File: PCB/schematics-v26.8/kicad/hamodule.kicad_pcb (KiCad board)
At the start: 4 copper layers, 129.6 x 83.3 mm, 203 parts, among them J1 GND|5V, J10 Tx|Rx, J11 Sda|Scl, J12 3|9, J13 13|12, J14 3.3v|GND|7|15, J15 2604-1104, J16 2604-1104, J17 TestPoint, J19 TestPoint, J2 2604-1102, J3 USB_C_Receptacle_USB2.0, J4 GND|3.3V, J5 Jumper 3.3v, J6 2604-1104, J7 2604-1104, J8 5v|GND|Do, J9 Screen, K1 AQG22205, K2 AQG22205, K3 AQG22205, K4 AQG22205, K5 AQG22205, K6 AQG22205, K7 AQG22205, K8 AQG22205, SW1 USB | PS, SW2 Reset, SW3 Boot, U1 LD1117AV33, U10 SN74LV1T34DBV, U11 ULN2803A, U12 TCAL6416, U14 74AHC1G04, U2 USBLC6-2SC6, U3 ESP32-S3-WROOM-2, U4 LDA210, U5 LDA210, U6 LDA210, U7 LDA210, U8 SHT4x, U9 SN74LVCH8T245

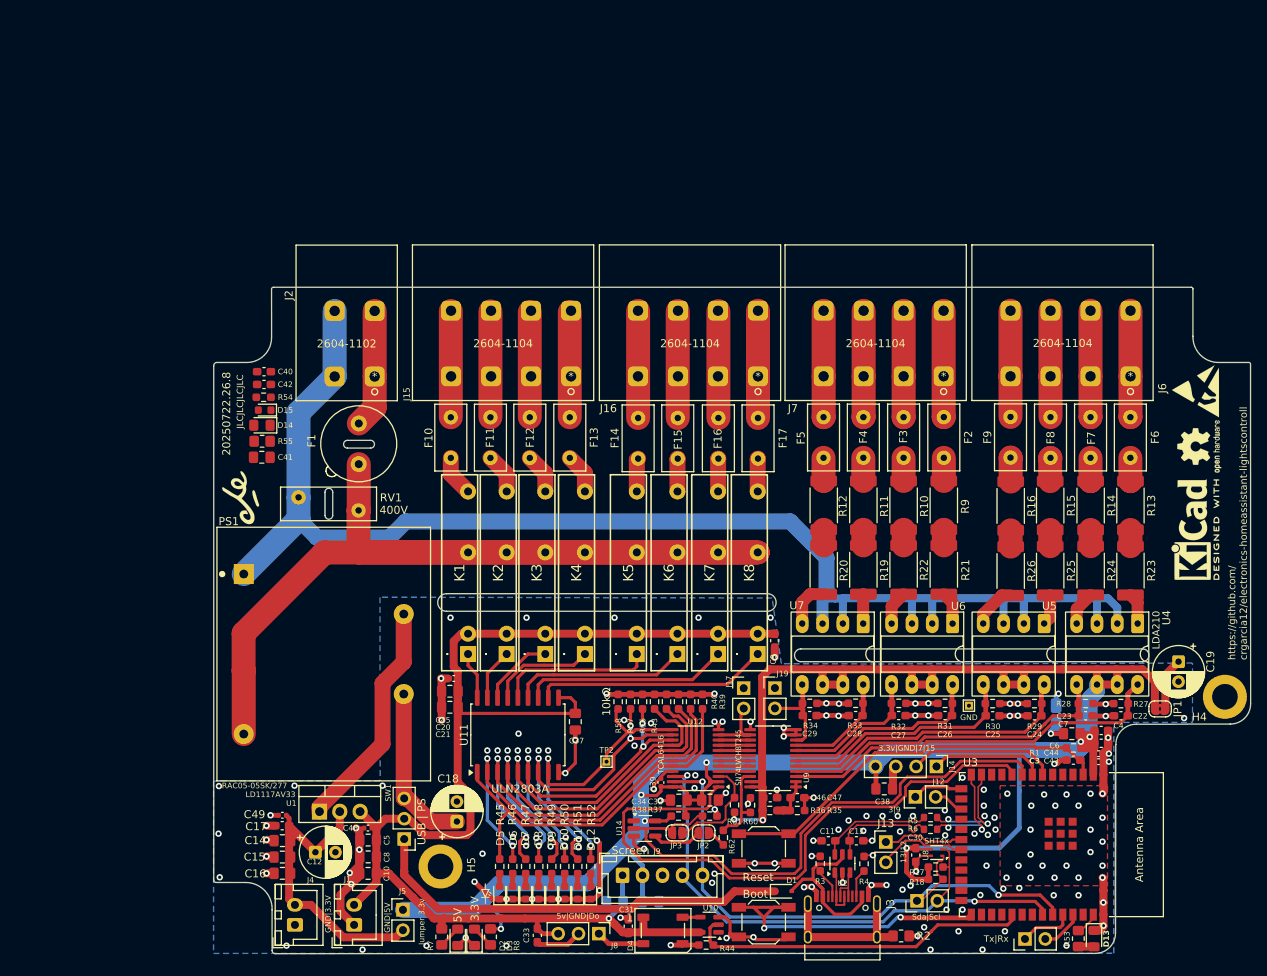
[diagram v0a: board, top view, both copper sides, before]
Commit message: Created only one project specific symbol library, one for footprints, and one for icons. Deleted all the rest from the components folder
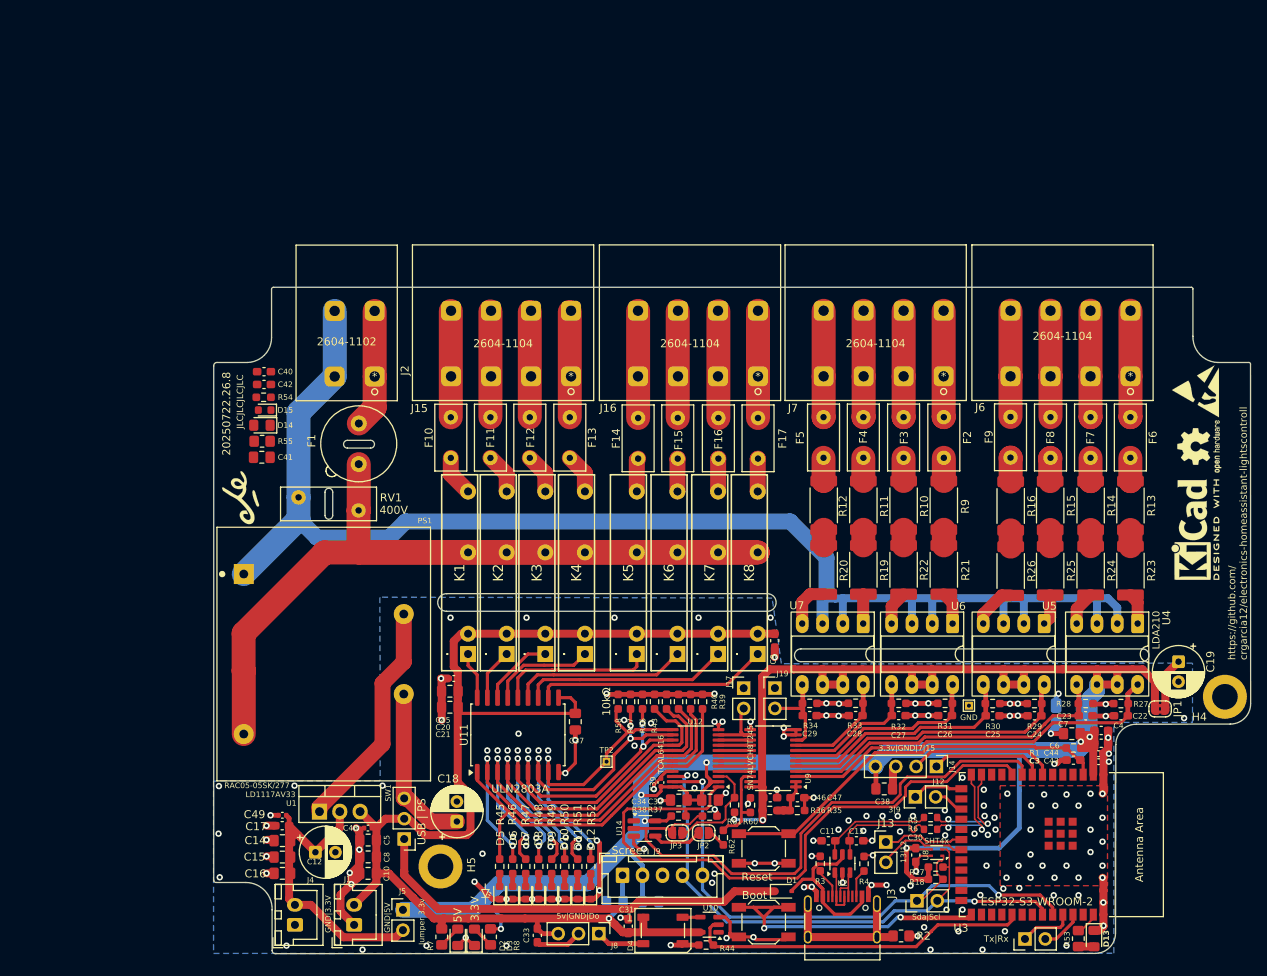
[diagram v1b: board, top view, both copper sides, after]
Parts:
- F10, F11, F12, F13, F14, F15, F16, F17, F2, F3, F4, F5, F6, F7, F8, F9: footprint RST-80-AMMO:FUSE_RST-1-BULK -> Hamodule_Footprints:FUSE_RST-1-BULK
- G1: footprint icons:depsi -> Hamodule_Icons_Footprints:depsi
- G10: footprint icons:che -> Hamodule_Icons_Footprints:che
- G2: footprint icons:flags -> Hamodule_Icons_Footprints:flags
- G3: footprint icons:qr_code_m -> Hamodule_Icons_Footprints:qr_code_m
- G4: footprint icons:led_6000dpi -> Hamodule_Icons_Footprints:led_6000dpi
- G5: footprint icons:danger1_negative -> Hamodule_Icons_Footprints:danger1_negative
- J15, J16, J6, J7: footprint wago-2604-1104:big_pads_2604-1104 -> Hamodule_Footprints:WAGO_2604-1104
- J2: footprint wago-2604-1102:big_pads_2604-1102 -> Hamodule_Footprints:WAGO-2604-1102
- J3: footprint usb-c:USB_C_Receptacle_HRO_TYPE-C-31-M-12 -> Connector_USB:USB_C_Receptacle_HRO_TYPE-C-31-M-12
- K1, K2, K3, K4, K5, K6, K7, K8: footprint AQG12205:AQG12205 -> Hamodule_Footprints:AQG12205
- PS1: footprint rac05-05sk:277 -> Hamodule_Footprints:RAC05-05SK_277
- SW2, SW3: footprint hamodule_SW_SPST_SKQG_WithStem:SW_SPST_SKQG_WithStem -> Button_Switch_SMD:SW_SPST_SKQG_WithStem
- U3: footprint Espressif:ESP32-S3-WROOM-2 -> Hamodule_Footprints:ESP32-S3-WROOM-2

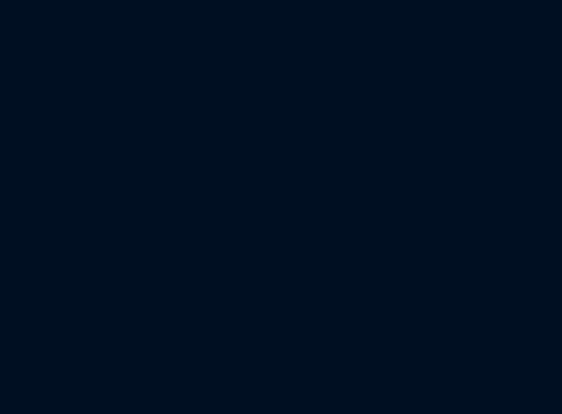
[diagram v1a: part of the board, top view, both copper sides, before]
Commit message: Created symbols for every image and logo, in order there are no warnings
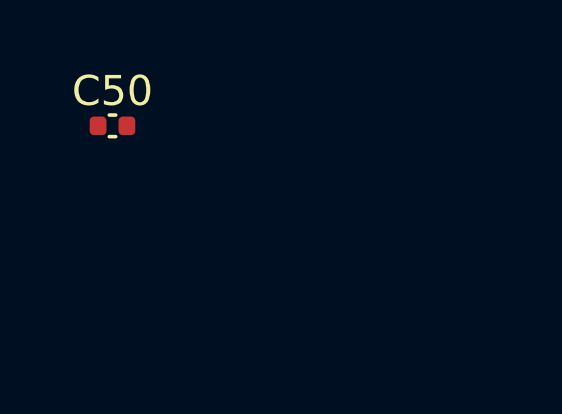
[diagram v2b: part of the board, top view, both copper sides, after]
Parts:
- added C50: 10uF, Capacitor_SMD:C_0402_1005Metric, F.Cu at (0.94, 0.48)
- G1: value LOGO -> Depsi
- G10: value LOGO -> Che
- G2: value LOGO -> Flags
- G3: value LOGO -> Qr Code; footprint Hamodule_Icons_Footprints:qr_code_m -> Hamodule_Icons_Footprints:qr_code
- G4: value LOGO -> Led; footprint Hamodule_Icons_Footprints:led_6000dpi -> Hamodule_Icons_Footprints:led
- G5: value LOGO -> Danger; footprint Hamodule_Icons_Footprints:danger1_negative -> Hamodule_Icons_Footprints:danger
- G6: value KiCad-Logo2_5mm_SilkScreen -> KiCad
- G7: value OSHW-Logo2_7.3x6mm_SilkScreen -> OSHW
- G8: value ESD-Logo_6.6x6mm_SilkScreen -> Esd

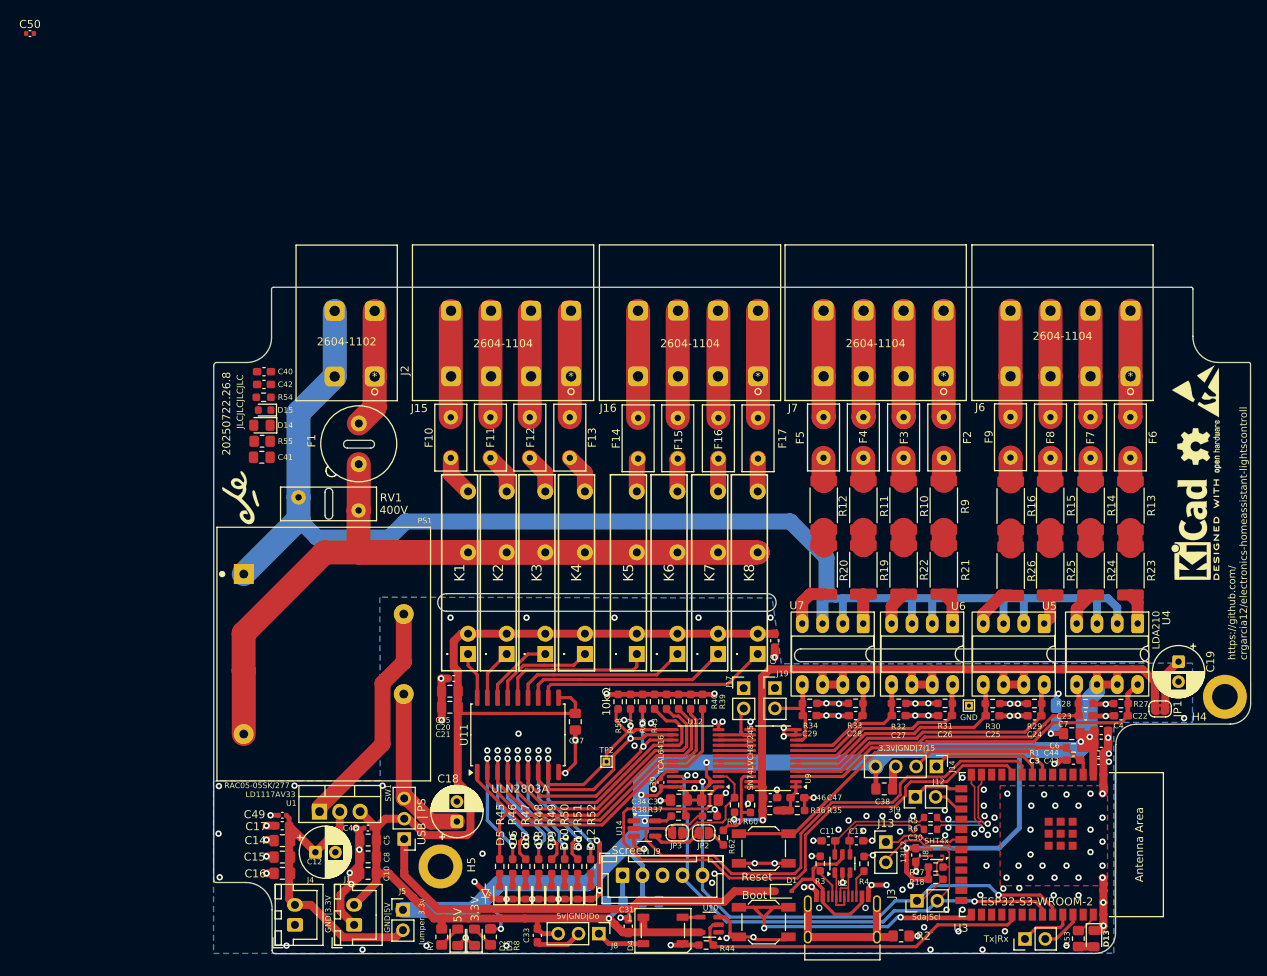
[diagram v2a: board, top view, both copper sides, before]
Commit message: Adding new spare part: C50 - 0402 capacitor
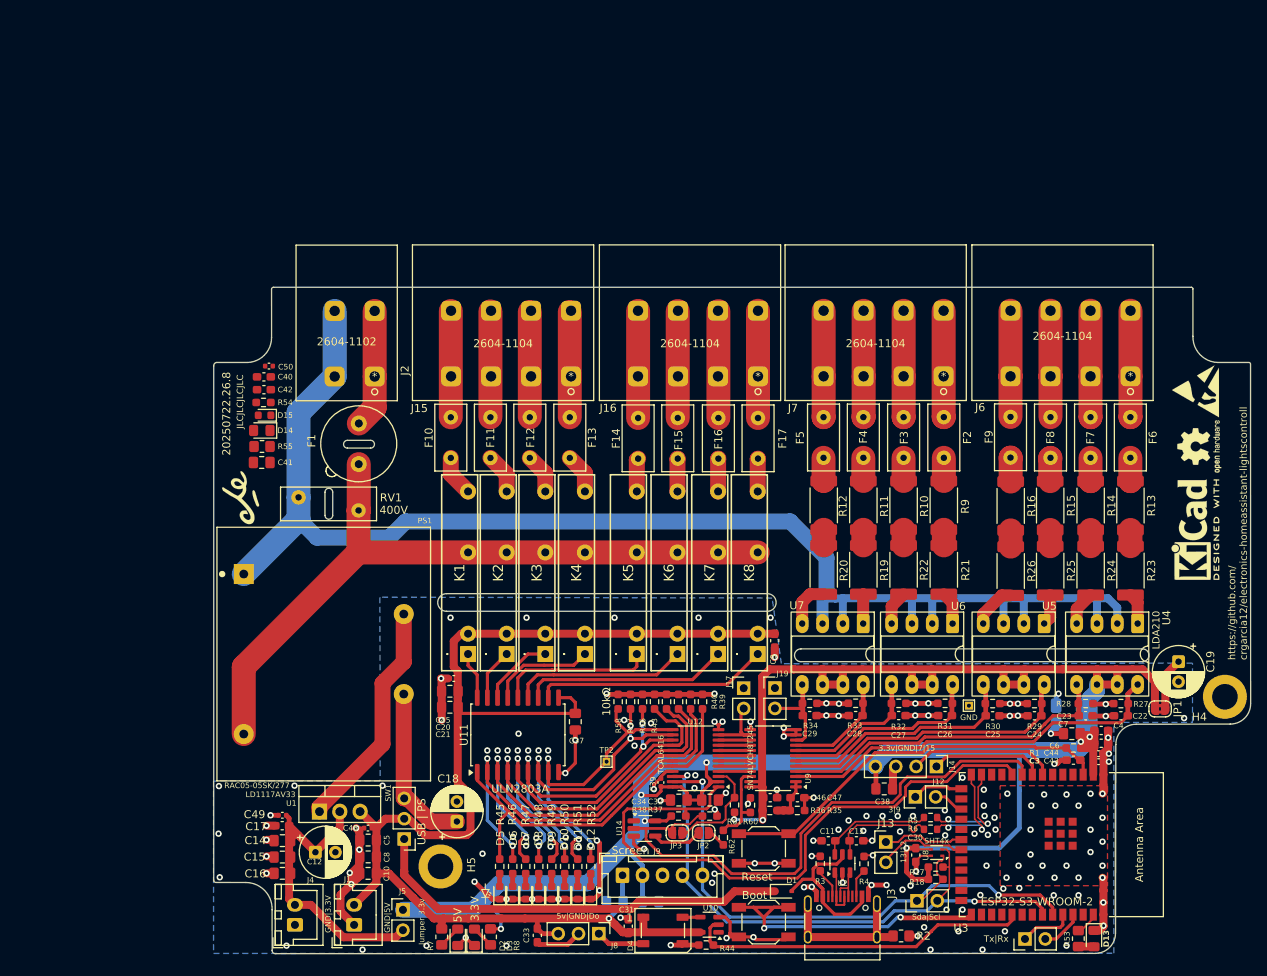
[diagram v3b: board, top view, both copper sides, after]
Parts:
- moved C50 51.2 mm to (30.8, 42.0)
- moved D15 0.65 mm to (30.2, 48.2)
- moved C41 0.65 mm to (29.9, 54.1)
- moved C40 0.65 mm to (30.2, 43.4)
- moved C42 0.65 mm to (30.2, 45.0)
- moved D14 0.65 mm to (29.9, 50.1)
- moved R54 0.65 mm to (30.1, 46.6)
- moved R55 0.65 mm to (29.9, 52.1)
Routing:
- net 220VAC(L): track 142.0 -> 89.6 mm
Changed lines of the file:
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@@
 	(footprint "Capacitor_SMD:C_0603_1608Metric_Pad1.08x0.95mm_HandSolder"
 		(layer "F.Cu")
-		(at 30.1875 42.75 180)
+		(at 30.175 43.4 180)
 		(descr "Capacitor SMD 0603 (1608 Metric), square (rectangular) end terminal, IPC-7351 nominal with elongated pad for handsoldering. (Body size source: IPC-SM-782 page 76, https://www.pcb-3d.com/wordpress/wp-content/uploads/ipc-sm-782a_amendment_1_and_2.pdf), generated with kicad-footprint-generator")
 		(tags "capacitor handsolder")
@@
 	(footprint "Capacitor_SMD:C_0402_1005Metric"
 		(layer "F.Cu")
-		(at 0.935 0.485)
+		(at 30.8075 42.05)
 		(descr "Capacitor SMD 0402 (1005 Metric), square (rectangular) end terminal, IPC-7351 nominal, (Body size source: IPC-SM-782 page 76, https://www.pcb-3d.com/wordpress/wp-content/uploads/ipc-sm-782a_amendment_1_and_2.pdf), generated with kicad-footprint-generator")
 		(tags "capacitor")
 		(property "Reference" "C50"
-			(at 0 -1.16 0)
+			(at 2.08 0.1 0)
 			(layer "F.SilkS")
 			(effects
 				(font
-					(size 1 1)
+					(size 0.7 0.7)
 					(thickness 0.15)
 				)
@@
 			(roundrect_rratio 0.25)
 			(net 174 "unconnected-(C50-Pad1)")
-			(pintype "passive")
+			(pintype "passive+no_connect")
 		)
 		(pad "2" smd roundrect
@@
 			(roundrect_rratio 0.25)
 			(net 175 "unconnected-(C50-Pad2)")
-			(pintype "passive")
+			(pintype "passive+no_connect")
 		)
 		(embedded_fonts no)
@@
 	(footprint "Capacitor_SMD:C_0603_1608Metric_Pad1.08x0.95mm_HandSolder"
 		(layer "F.Cu")
-		(at 30.1875 44.35)
+		(at 30.175 45)
 		(descr "Capacitor SMD 0603 (1608 Metric), square (rectangular) end terminal, IPC-7351 nominal with elongated pad for handsoldering. (Body size source: IPC-SM-782 page 76, https://www.pcb-3d.com/wordpress/wp-content/uploads/ipc-sm-782a_amendment_1_and_2.pdf), generated with kicad-footprint-generator")
 		(tags "capacitor handsolder")
@@
 	(footprint "Resistor_SMD:R_0805_2012Metric_Pad1.20x1.40mm_HandSolder"
 		(layer "F.Cu")
-		(at 29.95 51.45 180)
+		(at 29.9375 52.1 180)
 		(descr "Resistor SMD 0805 (2012 Metric), square (rectangular) end terminal, IPC-7351 nominal with elongated pad for handsoldering. (Body size source: IPC-SM-782 page 72, https://www.pcb-3d.com/wordpress/wp-content/uploads/ipc-sm-782a_amendment_1_and_2.pdf), generated with kicad-footprint-generator")
 		(tags "resistor handsolder")
@@
 	(footprint "LED_SMD:LED_0805_2012Metric_Pad1.15x1.40mm_HandSolder"
 		(layer "F.Cu")
-		(at 29.925 49.45 180)
+		(at 29.9125 50.1 180)
 		(descr "LED SMD 0805 (2012 Metric), square (rectangular) end terminal, IPC-7351 nominal, (Body size source: https://docs.google.com/spreadsheets/d/1BsfQQcO9C6DZCsRaXUlFlo91Tg2WpOkGARC1WS5S8t0/edit?usp=sharing), generated with kicad-footprint-generator")
 		(tags "LED handsolder")
@@
 	(footprint "Capacitor_SMD:C_0805_2012Metric_Pad1.18x1.45mm_HandSolder"
 		(layer "F.Cu")
-		(at 29.9125 53.45)
+		(at 29.9 54.1)
 		(descr "Capacitor SMD 0805 (2012 Metric), square (rectangular) end terminal, IPC-7351 nominal with elongated pad for handsoldering. (Body size source: IPC-SM-782 page 76, https://www.pcb-3d.com/wordpress/wp-content/uploads/ipc-sm-782a_amendment_1_and_2.pdf, https://docs.google.com/spreadsheets/d/1BsfQQcO9C6DZCsRaXUlFlo91Tg2WpOkGARC1WS5S8t0/edit?usp=sharing), generated with kicad-footprint-generator")
 		(tags "capacitor handsolder")
@@
 	(footprint "Resistor_SMD:R_0603_1608Metric_Pad0.98x0.95mm_HandSolder"
 		(layer "F.Cu")
-		(at 30.1375 45.95 180)
+		(at 30.125 46.6 180)
 		(descr "Resistor SMD 0603 (1608 Metric), square (rectangular) end terminal, IPC-7351 nominal with elongated pad for handsoldering. (Body size source: IPC-SM-782 page 72, https://www.pcb-3d.com/wordpress/wp-content/uploads/ipc-sm-782a_amendment_1_and_2.pdf), generated with kicad-footprint-generator")
 		(tags "resistor handsolder")
@@
 	(footprint "LED_SMD:LED_0603_1608Metric"
 		(layer "F.Cu")
-		(at 30.2625 47.55 180)
+		(at 30.25 48.2 180)
 		(descr "LED SMD 0603 (1608 Metric), square (rectangular) end terminal, IPC-7351 nominal, (Body size source: http://www.tortai-tech.com/upload/download/2011102023233369053.pdf), generated with kicad-footprint-generator")
 		(tags "LED")
@@
 	)
 	(segment
-		(start 42.027 54.3052)
-		(end 42.027 60.0718)
-		(width 3)
-		(layer "F.Cu")
-		(net 1)
-	)
-	(segment
-		(start 91.9 65.3439)
-		(end 37.7547 65.3439)
+		(start 27.656 79.644)
+		(end 27.656 88.0466)
 		(width 3)
 		(layer "F.Cu")
@@
 	)
 	(segment
-		(start 37.5412 65.5574)
-		(end 27.6352 75.4634)
-		(width 3)
-		(layer "F.Cu")
-		(net 1)
-	)
-	(segment
-		(start 27.6352 80.1288)
-		(end 27.6352 75.4634)
-		(width 3)
-		(layer "F.Cu")
-		(net 1)
-	)
-	(segment
-		(start 37.7547 65.3439)
-		(end 37.5412 65.5574)
+		(start 42.027 54.3052)
+		(end 42.027 60.0718)
 		(width 3)
 		(layer "F.Cu")
@@
 	)
 	(segment
-		(start 27.656 80.1496)
-		(end 27.6352 80.1288)
+		(start 42.0347 65.3439)
+		(end 41.9561 65.3439)
 		(width 3)
 		(layer "F.Cu")
@@
 	)
 	(segment
-		(start 27.656 88.0466)
-		(end 27.656 80.1496)
+		(start 41.9561 65.3439)
+		(end 27.656 79.644)
 		(width 3)
 		(layer "F.Cu")
